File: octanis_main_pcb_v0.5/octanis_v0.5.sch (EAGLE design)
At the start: 103 parts, among them IC1 BME280, IC2 BNO055A, Q1 32.768kHz, Q2 32.768kHz, U1 MSP432, U10 INA213, U11 INA213, U12 MAX6001SOT-23, U2 TPS61232, U3 DRV8836DSSR, U4 DRV8836DSSR, U5 DRV8836DSSR, U6 DRV8836DSSR, U7 SST25VF064C, U8 INA213, U9 INA213

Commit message: renumbered parts in mainboard
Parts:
- removed LED0: LED0, adafruit:LEDCHIPLED_0603
- removed RPUC, RPUD: 4.7k, rcl:R-EU_R0603
- added LED2: LED1, adafruit:LEDCHIPLED_0603
- added R19: 10k, rcl:R-EU_R0603
- added R20: 6.8k, rcl:R-EU_R0603
- C1: value 100n -> 10u; device rcl:C-EUC0402 -> rcl:CPOL-EUA/3216-18R
- C10, C30: value 10u -> 470n; device rcl:CPOL-EUA/3216-18R -> rcl:C-EUC0603
- C12, C29: value 100n -> 470n
- C13: value 100n -> 10u; device rcl:C-EUC0603 -> rcl:CPOL-EUA/3216-18R
- C15: value 1n -> 10u; device rcl:C-EUCM0402 -> rcl:CPOL-EUA/3216-18R
- C16: value 12p -> 100n; device rcl:C-EUC0603 -> rcl:C-EUC0402
- C19, C23: value 100n -> 12p
- C2: value 100n -> 22uF
- C20: value 120n -> 100n
- C21, C24: value 10n -> 100n
- C22: value 12p -> 120n; device rcl:C-EUC0402 -> rcl:C-EUC0603
- C25: value 10u -> 12p; device rcl:CPOL-EUA/3216-18R -> rcl:C-EUC0402
- C26: value 470n -> 100n; device rcl:C-EUC0603 -> rcl:C-EUC0402
- C3, C6: value 22uF -> 100n
- C31, C32: value 10n -> 470n
- C33, C34, C35, C36: value 470n -> 10n
- C4: value 10nF -> 22uF
- C5: value 22uF -> 10nF
- C7: value 3 x 22uF -> 22uF
- C8: value 470n -> 1n; device rcl:C-EUC0603 -> rcl:C-EUCM0402
- C9: value 12p -> 3 x 22uF; device rcl:C-EUC0402 -> rcl:C-EUC0603
- LED1: value LED1 -> LED0
- R1: value 10k -> 4.7k
- R10: value 91k 0.1% ±25 ppm/°C -> 10k; device rcl:R-EU_R0402 -> rcl:R-EU_R0603
- R11: value 10k -> 0R; device rcl:R-EU_R0603 -> rcl:R-EU_R0402
- R13: value 47k -> 10k; device rcl:R-EU_RM0402 -> rcl:R-EU_R0603
- R14: value 6.8k -> 91k 0.1% ±25 ppm/°C; device rcl:R-EU_R0603 -> rcl:R-EU_R0402
- R16: value 10k -> 6.8k
- R17: value 6.8k -> 10k
- R2: value 1M -> 1k
- R3: value 1M -> 4.7k
- R4: value 1k -> 1M
- R5: value 10k -> 1M
- R7: value 0R -> 1k; device rcl:R-EU_R0402 -> rcl:R-EU_R0603
- R8: value 1k -> 47k; device rcl:R-EU_R0603 -> rcl:R-EU_RM0402
- RS1: value RS1 -> RS4
- RS2: value RS2 -> RS3
- RS3: value RS3 -> RS2
- RS4: value RS4 -> RS1
- U1: value MSP432 -> TPS61232; device MSP-EXP432:MSP432 -> texasinstruments:TPS61232
- U12: value MAX6001SOT-23 -> INA213; device Octanis1:MAX6001SOT-23 -> Octanis1_EPS:INA213
- U2: value TPS61232 -> DRV8836DSSR; device texasinstruments:TPS61232 -> DRV8834:DRV8836DSSR
- U4: value DRV8836DSSR -> MSP432; device DRV8834:DRV8836DSSR -> MSP-EXP432:MSP432
- U5: value DRV8836DSSR -> SST25VF064C; device DRV8834:DRV8836DSSR -> BertaLib:SST25VF064C
- U7: value SST25VF064C -> DRV8836DSSR; device BertaLib:SST25VF064C -> DRV8834:DRV8836DSSR
- U8: value INA213 -> MAX6001SOT-23; device Octanis1_EPS:INA213 -> Octanis1:MAX6001SOT-23
- renumbered JP4 to JP2, JP5 to JP1, LED_J1 to LED_J101, LED_J2 to LED_J100, M1/M2 to M1/M1, M3/M4 to M3/M1, M5/M6 to M5/M1, M7/M8 to M7/M1, RX2/TX2 to RX2/TX1, RX3/TX3 to RX3/TX1, U$2 to U$100, U$4 to U$1
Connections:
- net +3V3: now also C13.+, C2.1, C20.2, C21.1, C22.1, C24.1, C6.1, R1.2, R10.2, R12.1, R17.2, R19.2, R3.2, R4.2, R8.2, U1.VIN, U4.DVCC1, U4.DVCC2, U5.HOLD, U5.VCC, U5.WP, U8.IN; no longer C13.1, C14.1, C19.2, C20.1, C29.1, C3.1, C30.+, R1.1, R12.2, R16.2, R2.2, R5.2, R7.2, RPUC.2, RPUD.2, U1.DVCC1, U1.DVCC2, U12.IN, U2.VIN, U7.HOLD, U7.VCC, U7.WP
- net +5V: now also C1.+, C3.1, C4.1, C9.1, R5.2, U1.FB, U1.VOUT; no longer C10.+, C2.1, C5.1, C6.1, R3.2, U2.FB, U2.VOUT
- net 5VEN: now also R4.1, U1.EN, U4.P2.1/PM_UCA1CLK; no longer R2.1, U1.P2.1/PM_UCA1CLK, U2.EN
- net A0: now also U4.P5.5/A0; no longer U1.P5.5/A0
- net A1: now also U4.P5.4/A1; no longer U1.P5.4/A1
- net A10: now also U4.P4.3/MCLK/RTCCLK/A10; no longer U1.P4.3/MCLK/RTCCLK/A10
- net A11: now also U4.P4.2/ACLK/TA2CLK/A11; no longer U1.P4.2/ACLK/TA2CLK/A11
- net A12: now also U4.P4.1/A12; no longer U1.P4.1/A12
- net A13: now also U4.P4.0/A13; no longer U1.P4.0/A13
- net A14: now also U4.P6.1/A14; no longer U1.P6.1/A14
- net A15: now also U4.P6.0/A15; no longer U1.P6.0/A15
- net A16: now also U4.P9.1/A16; no longer U1.P9.1/A16
- net A17: now also U4.P9.0/A17; no longer U1.P9.0/A17
- net A18: now also U4.P8.7/A18; no longer U1.P8.7/A18
- net A2: now also U4.P5.3/A2; no longer U1.P5.3/A2
- net A20: now also C32.2, R20.1, U4.P8.5/A20; no longer C35.2, R17.1, U1.P8.5/A20
- net A20UNF: now also R20.2, U9.OUT; no longer R17.2, U11.OUT
- net A21: now also C28.2, U4.P8.4/A21; no longer C36.2, U1.P8.4/A21
- net A22: now also C29.2, R16.1, U4.P8.3/TA3CLK/A22; no longer C34.2, R15.1, U1.P8.3/TA3CLK/A22
- net A22UNF: now also R16.2, U11.OUT; no longer R15.2, U9.OUT
- net A23: now also C27.2, R15.1, U4.P8.2/TA3.2/A23; no longer C33.2, R14.1, U1.P8.2/TA3.2/A23
- net A23UNF: now also R15.2, U12.OUT; no longer R14.2, U8.OUT
- net A3: now also U4.P5.2/A3; no longer U1.P5.2/A3
- net A4: now also U4.P5.1/A4; no longer U1.P5.1/A4
- net A5: now also U4.P5.0/A5; no longer U1.P5.0/A5
- net A6: now also U4.P4.7/A6; no longer U1.P4.7/A6
- net A7: now also U4.P4.6/A7; no longer U1.P4.6/A7
- net A8: now also U4.P4.5/A8; no longer U1.P4.5/A8
- net A9: now also U4.P4.4/HSMCLK/SVMHOUT/A9; no longer U1.P4.4/HSMCLK/SVMHOUT/A9
- net ACCEL_INT: now also U4.P3.5/PM_UCB2CLK; no longer U1.P3.5/PM_UCB2CLK
- net ACCEL_N_BOOTLD: now also R13.1; no longer R5.1
- net ACCEL_N_RST: now also R12.2; no longer R1.2
- net AGND: now also C16.2, C26.2, C27.1, C28.1, C29.1, R14.2, U4.AVSS1, U4.AVSS2, U4.AVSS3; no longer C1.2, C21.1, C23.2, C24.1, C31.1, R10.2, U1.AVSS1, U1.AVSS2, U1.AVSS3
- net AVCC: now also C16.1, C26.1, R11.1, U4.AVCC1, U4.AVCC2; no longer C1.1, C23.1, R7.1, U1.AVCC1, U1.AVCC2
- net CURR_SENSE_EN: now also C33.2, C34.2, C35.2, C36.2, U12.VCC, U4.P8.6/A19; no longer C21.2, C24.2, C31.2, C32.2, U1.P8.6/A19, U8.VCC
- net GND: now also C10.1, C13.-, C14.1, C15.-, C19.2, C2.2, C20.1, C21.2, C22.2, C23.1, C24.2, C25.1, C30.1, C31.1, C8.2, C9.2, R6.1, R7.1, U1.GND, U1.GND1, U1.GND2, U1.GND3, U1.GND4, U1.GND5, U2.EPAD, U4.DVSS1, U4.DVSS2, U4.DVSS3, U4.P5.7/TA2.2/VREF-/VEREF-/C1.6, U7.EPAD; no longer C13.2, C14.2, C15.2, C16.2, C19.1, C20.2, C22.1, C25.-, C26.1, C27.1, C28.1, C29.2, C3.2, C30.-, C8.1, C9.1, R8.1, R9.1, U1.DVSS1, U1.DVSS2, U1.DVSS3, U1.P5.7/TA2.2/VREF-/VEREF-/C1.6, U2.GND1, U2.GND2, U2.GND3, U2.GND4, U2.GND5, U4.EPAD, U4.GND, U5.EPAD
- net HX1_DATA: now also U4.P1.4/UCB0STE; no longer U1.P1.4/UCB0STE
- net HX1_EN: now also U4.P1.5/UCB0CLK; no longer U1.P1.5/UCB0CLK
- net IND: now also U1.SW; no longer U2.SW
- net LED0: now also LED1.A, U4.P10.0/UCB3STE; no longer LED0.A, U1.P10.0/UCB3STE
- net LED1: now also LED2.A, U4.P10.1/UCB3CLK; no longer LED1.A, U1.P10.1/UCB3CLK
- net M1234SLEEP: now also R10.1, U2.MODE, U2.NSLEEP, U4.P2.2/PM_UCA1RXD/PM_UCA1SOMI; no longer R12.1, U1.P2.2/PM_UCA1RXD/PM_UCA1SOMI, U4.MODE, U4.NSLEEP
- net M1IN1: now also U2.AIN1_/_APHASE, U4.P2.3/PM_UCA1TXD/PM_UCA1SIMO; no longer U1.P2.3/PM_UCA1TXD/PM_UCA1SIMO, U3.AIN1_/_APHASE
- net M1IN2: now also U2.AIN2_/_AENBL, U4.P2.4/PM_TA0.1; no longer U1.P2.4/PM_TA0.1, U3.AIN2_/_AENBL
- net M2IN1: now also U2.BIN1_/_BPHASE, U4.P2.5/PM_TA0.2; no longer U1.P2.5/PM_TA0.2, U3.BIN1_/_BPHASE
- net M2IN2: now also U2.BIN2_/_BENBL, U4.P2.6/PM_TA0.3; no longer U1.P2.6/PM_TA0.3, U3.BIN2_/_BENBL
- net M3IN1: now also U3.AIN1_/_APHASE, U4.P2.7/PM_TA0.4; no longer U1.P2.7/PM_TA0.4, U4.AIN1_/_APHASE
- net M3IN2: now also U3.AIN2_/_AENBL, U4.P10.4/TA3.0/C0.7; no longer U1.P10.4/TA3.0/C0.7, U4.AIN2_/_AENBL
- net M4IN1: now also U3.BIN1_/_BPHASE, U4.P10.5/TA3.1/C0.6; no longer U1.P10.5/TA3.1/C0.6, U4.BIN1_/_BPHASE
- net M4IN2: now also U3.BIN2_/_BENBL, U4.P7.4/PM_TA1.4/C0.5; no longer U1.P7.4/PM_TA1.4/C0.5, U4.BIN2_/_BENBL
- net M5678SLEEP: now also R17.1, U4.P2.0/PM_UCA1STE, U7.MODE, U7.NSLEEP; no longer R11.1, U1.P2.0/PM_UCA1STE, U5.MODE, U5.NSLEEP
- net M5IN1: now also U4.P7.5/PM_TA1.3/C0.4, U7.AIN1_/_APHASE; no longer U1.P7.5/PM_TA1.3/C0.4, U5.AIN1_/_APHASE
- net M5IN2: now also U4.P7.6/PM_TA1.2/C0.3, U7.AIN2_/_AENBL; no longer U1.P7.6/PM_TA1.2/C0.3, U5.AIN2_/_AENBL
- net M5OUT1: now also RS4.I1, U7.AOUT1; no longer RS1.I1, U5.AOUT1
- net M6IN1: now also U4.P8.0/UCB3STE/TA1.0/C0.1, U7.BIN1_/_BPHASE; no longer U1.P8.0/UCB3STE/TA1.0/C0.1, U5.BIN1_/_BPHASE
- net M6IN2: now also U4.P7.7/PM_TA1.1/C0.2, U7.BIN2_/_BENBL; no longer U1.P7.7/PM_TA1.1/C0.2, U5.BIN2_/_BENBL
- net M7IN1: now also U4.P8.1/UCB3CLK/TA2.0/C0.0; no longer U1.P8.1/UCB3CLK/TA2.0/C0.0
- net M7IN2: now also U4.P3.0/PM_UCA2STE; no longer U1.P3.0/PM_UCA2STE
- net M8IN1: now also U4.P3.1/PM_UCA2CLK; no longer U1.P3.1/PM_UCA2CLK
- net M8IN2: now also U4.P3.4/PM_UCB2STE; no longer U1.P3.4/PM_UCB2STE
- net N$1: now also C14.2, C15.+, U4.VCORE; no longer C18.2, C25.+, U1.VCORE
- net N$10: now also C25.2, U4.PJ.1/LFXOUT; no longer C9.2, U1.PJ.1/LFXOUT
- net N$13: now also U3.AOUT1; no longer U4.AOUT1
- net N$14: now also R2.1; no longer R6.1
- net N$15: now also RS4.V2, U12.IN-; no longer RS1.V2, U8.IN-
- net N$17: now also RS4.V1, U12.IN+; no longer RS1.V1, U8.IN+
- net N$18: now also C18.2; no longer C12.2
- net N$19: now also C19.1; no longer C16.1
- net N$2: now also R5.1, U1.PG; no longer R3.1, U2.PG
- net N$21: now also RS4.I2; no longer RS1.I2
- net N$23: now also RS3.V1, U11.IN+; no longer RS2.V1, U9.IN+
- net N$24: now also RS3.V2, U11.IN-; no longer RS2.V2, U9.IN-
- net N$25: now also RS3.I1, U7.BOUT1; no longer RS2.I1, U5.BOUT1
- net N$26: now also R9.1; no longer R4.1
- net N$27: now also RS3.I2; no longer RS2.I2
- net N$28: now also RS2.V2; no longer RS3.V2
- net N$29: now also RS2.V1; no longer RS3.V1
- net N$30: now also RS1.V2, U9.IN-; no longer RS4.V2, U11.IN-
- net N$31: now also RS1.V1, U9.IN+; no longer RS4.V1, U11.IN+
- net N$32: now also RS2.I2; no longer RS3.I2
- net N$33: now also R14.1, U4.DCOR; no longer R10.1, U1.DCOR
- net N$34: now also U4.VSW; no longer U1.VSW
- net N$35: now also RS1.I1; no longer RS4.I1
- net N$36: now also RS2.I1; no longer RS3.I1
- net N$37: now also RS1.I2; no longer RS4.I2
- net N$38: now also U7.AOUT2; no longer U5.AOUT2
- net N$39: now also U3.AOUT2; no longer U4.AOUT2
- net N$4: now also R9.2; no longer R4.2
- net N$40: now also U3.BOUT1; no longer U4.BOUT1
- net N$41: now also U3.BOUT2; no longer U4.BOUT2
- net N$42: now also C5.1, U1.SS; no longer C4.1, U2.SS
- net N$43: now also U7.BOUT2; no longer U5.BOUT2
- net N$44: now also R2.2; no longer R6.2
- net N$49: now also U2.AOUT1; no longer U3.AOUT1
- net N$5: now also LED1.C, R7.2; no longer LED0.C, R8.2
- net N$50: now also U2.AOUT2; no longer U3.AOUT2
- net N$51: now also U2.BOUT1; no longer U3.BOUT1
- net N$52: now also U2.BOUT2; no longer U3.BOUT2
- net N$6: now also LED2.C, R6.2; no longer LED1.C, R9.2
- net N$76: now also U4.SWDIOTMS; no longer U1.SWDIOTMS
- net N$77: now also U4.SWCLKTCK; no longer U1.SWCLKTCK
- net N$8: now also C23.2, U4.PJ.0/LFXIN; no longer C22.2, U1.PJ.0/LFXIN
- net P1.0: now also U4.P1.0/UCA0STE; no longer U1.P1.0/UCA0STE
- net P1.1: now also U4.P1.1/UCA0CLK; no longer U1.P1.1/UCA0CLK
- net P10.2: now also U4.P10.2/UCB3SIMO/UCB3SDA; no longer U1.P10.2/UCB3SIMO/UCB3SDA
- net P10.3: now also U4.P10.3UCB3SOMI/UCB3SCL; no longer U1.P10.3UCB3SOMI/UCB3SCL
- net P3.6: now also U4.P3.6/PM_UCB2SIMO/PM_UCB2SDA; no longer U1.P3.6/PM_UCB2SIMO/PM_UCB2SDA
- net P3.7: now also U4.P3.7/PM_UCB2SOMI/PM_UCB2SCL; no longer U1.P3.7/PM_UCB2SOMI/PM_UCB2SCL
- net P6.6: now also U4.P6.6/TA2.3/UCB3SIMO/UCB3SDA/C1.1; no longer U1.P6.6/TA2.3/UCB3SIMO/UCB3SDA/C1.1
- net P6.7: now also U4.P6.7/TA2.4/UCB3SOMI/UCB3SCL/C1.0; no longer U1.P6.7/TA2.4/UCB3SOMI/UCB3SCL/C1.0
- net P7.0: now also U4.P7.0/PM_SMCLK/PM_DMAE0; no longer U1.P7.0/PM_SMCLK/PM_DMAE0
- net P7.1: now also U4.P7.1/PM_C0OUT/PM_TA0CLK; no longer U1.P7.1/PM_C0OUT/PM_TA0CLK
- net P7.2: now also U4.P7.2/PM_C1OUT/PM_TA1CLK; no longer U1.P7.2/PM_C1OUT/PM_TA1CLK
- net P7.3: now also U4.P7.3/PM_TA0.0; no longer U1.P7.3/PM_TA0.0
- net P9.2: now also U4.P9.2/TA3.3; no longer U1.P9.2/TA3.3
- net P9.3: now also U4.P9.3/TA3.4; no longer U1.P9.3/TA3.4
- net P9.4: now also U4.P9.4/UCA3STE; no longer U1.P9.4/UCA3STE
- net P9.5: now also U4.P9.5/UCA3CLK; no longer U1.P9.5/UCA3CLK
- net PJ.2: now also U4.PJ.2/HFXOUT; no longer U1.PJ.2/HFXOUT
- net PJ.3: now also U4.PJ.3/HFXIN; no longer U1.PJ.3/HFXIN
- net PJ.4: now also U4.PJ.4/TDI/ADC14CLK; no longer U1.PJ.4/TDI/ADC14CLK
- net PJ.5: now also U4.PJ.5/TDO/SWO; no longer U1.PJ.5/TDO/SWO
- net RFGND: now also C1.-, C3.2; no longer C10.-, C2.2
- net RST_N: now also C8.1, R8.1, U4.RSTN/NMI; no longer C15.1, R13.1, U1.RSTN/NMI
- net RX0: now also U4.P1.2/UCA0RXD/UCA0SOMI; no longer U1.P1.2/UCA0RXD/UCA0SOMI
- net RX2: now also U4.P3.2/PM_UCA2RXD/PM_UCA2SOMI; no longer U1.P3.2/PM_UCA2RXD/PM_UCA2SOMI
- net RX3: now also U4.P9.6/UCA3RXD/UCA3SOMI; no longer U1.P9.6/UCA3RXD/UCA3SOMI
- net SCL: now also R1.1, U4.P1.7/UCB0SOMI/UCB0SCL; no longer RPUD.1, U1.P1.7/UCB0SOMI/UCB0SCL
- net SDA: now also R3.1, U4.P1.6/UCB0SIMO/UCB0SDA; no longer RPUC.1, U1.P1.6/UCB0SIMO/UCB0SDA
- net SPI_EXTSLAVE_TE: now also U4.P6.2/UCB1STE/C1.5; no longer U1.P6.2/UCB1STE/C1.5
- net SPI_FLASH_CS: now also R19.1, U4.P5.6/TA2.1/VREF+/VEREF+/C1.7, U5.CS; no longer R16.1, U1.P5.6/TA2.1/VREF+/VEREF+/C1.7, U7.CS
- net SPI_MISO: now also U4.P6.5/UCB1SOMI/UCB1SCL/C1.2, U5.MISO; no longer U1.P6.5/UCB1SOMI/UCB1SCL/C1.2, U7.MISO
- net SPI_MOSI: now also U4.P6.4/UCB1SIMO/UCB1SDA/C1.3, U5.MOSI; no longer U1.P6.4/UCB1SIMO/UCB1SDA/C1.3, U7.MOSI
- net SPI_SCK: now also U4.P6.3/UCB1CLK/C1.4, U5.SCK; no longer U1.P6.3/UCB1CLK/C1.4, U7.SCK
- net TX0: now also U4.P1.3/UCA0TXD/UCA0SIMO; no longer U1.P1.3/UCA0TXD/UCA0SIMO
- net TX2: now also U4.P3.3/PM_UCA2TXD/PM_UCA2SIMO; no longer U1.P3.3/PM_UCA2TXD/PM_UCA2SIMO
- net TX3: now also U4.P9.7/UCA3TXD/UCA3SIMO; no longer U1.P9.7/UCA3TXD/UCA3SIMO
- net VREF_M: now also U12.REF, U8.OUT; no longer U12.OUT, U8.REF
- net V_MOTOR: now also C10.2, C12.2, U2.VCC; no longer C27.2, C28.2, U4.VCC
- net V_MOTOR2: now also C30.2, C31.2, U7.VCC; no longer C26.2, C8.2, U5.VCC
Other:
- moved on the sheet: C11, C12, C14, C16, C18, C19, C2, C20, C21, C22, C23, C24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

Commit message: added RN2483 LoRa module, separated 3v supply for motors and 5V converter from main circuit supply. *
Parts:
- removed C1: 10u, rcl:CPOL-EUA/3216-18R
- removed C3: 100n, rcl:C-EUC0603
- removed MOT_J, RF_J: (no value), jumper:SJ
- removed PROG: (no value), Headerlibrary:PINHD-1X72MM
- removed R10, R17: 10k, rcl:R-EU_R0603
- removed RX3/TX1: (no value), pinhead:PINHD-2X2
- removed U$1: HX1EXTERNALMOUNT, Octanis1:HX1EXTERNALMOUNT
- added 433MHZ, 868MHZ, LORA_RST_N: (no value), Headerlibrary:PINHD-1X1
- added J1: (no value), Seeed-OPL-Connector:SMD-BLUE-FEMALE-HEADER-VERT(2X3P-2.54)
- added MOT_J1: (no value), jumper:SJ
- added R21: 100k, rcl:R-EU_R0603
- added RX1/TX1: (no value), pinhead-2:PINHD-1X04_2.54-S
- added U13: RN2483, Octanis1:RN2483
- added VMOT_SEL2: 3V3 V_Motor 5V, jumper:SJ2W
- JP1: device pinhead:PINHD-2X2 -> Headerlibrary:PINHD-1X72MM_SMD
- R12, R13: value 10k -> 100k
- renumbered M1/M1 to M1/M2, M3/M1 to M3/M4, RX2/TX1 to RX2/TX2
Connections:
- removed net HX1_DATA: U$1.TXD, U4.P1.4/UCB0STE
- removed net HX1_EN: U$1.EN, U4.P1.5/UCB0CLK
- removed net P1.1: DIGITAL_IO.21, U4.P1.1/UCA0CLK
- removed net P10.3: DIGITAL_IO.22, U4.P10.3UCB3SOMI/UCB3SCL
- removed net P3.6: DIGITAL_IO.5, U4.P3.6/PM_UCB2SIMO/PM_UCB2SDA
- removed net RFGND: C1.-, C3.2, RF_J.2, U$1.0V, U$1.RFGND, U$1.RFGND2
- new net 3V3_MODULE2: C2.1, JP2.10, JP2.9, L1.1, R4.2, U1.VIN, U8.IN, VMOT_SEL.1, VMOT_SEL2.1
- new net ANT433: 433MHZ.1, U13.P$25
- new net ANT868: 868MHZ.1, U13.P$23
- new net EXT_LIGHTNING_INT: J1.6, U4.P1.4/UCB0STE
- new net EXT_UV_EN: J1.1, U4.P1.5/UCB0CLK
- new net LORA_RST_N: LORA_RST_N.1, R21.1, U13.P$32
- new net N$20: MOT_J1.1, R4.1, U1.EN
- new net P5.7: DIGITAL_IO.5, U4.P5.7/TA2.2/VREF-/VEREF-/C1.6
- new net RX1: RX1/TX1.3, U4.P2.2/PM_UCA1RXD/PM_UCA1SOMI
- new net TX1: RX1/TX1.2, U4.P2.3/PM_UCA1TXD/PM_UCA1SIMO
- net +3V3: now also DIGITAL_IO.21, J1.2, JP1.7, JP2.3, JP2.4, R21.2, RX1/TX1.4, U13.P$12, U13.P$34; no longer C2.1, JP1.1, JP2.10, JP2.7, JP2.8, JP2.9, L1.1, PROG.7, R10.2, R17.2, R4.2, RX2/TX2.1, RX3/TX1.3, U1.VIN, U8.IN, VMOT_SEL.1
- net +5V: now also RX2/TX2.4, VMOT_SEL2.3; no longer C1.+, C3.1, MOT_J.2, U$1.VCC
- net 5VEN: now also MOT_J1.2; no longer R4.1, U1.EN
- net ACCEL_INT: now also U4.P1.1/UCA0CLK; no longer U4.P3.5/PM_UCB2CLK
- net ACCEL_N_RST: now also U4.P10.3UCB3SOMI/UCB3SCL
- net GND: now also DIGITAL_IO.22, J1.5, JP1.1, JP2.7, JP2.8, RX1/TX1.1, RX2/TX2.1, U13.P$1, U13.P$11, U13.P$20, U13.P$21, U13.P$22, U13.P$24, U13.P$26, U13.P$27, U13.P$28, U13.P$33, U13.P$41, U13.P$47, U13.P$8; no longer JP1.2, JP2.3, JP2.4, PROG.1, RF_J.1, RX2/TX2.4, RX3/TX1.1, U4.P5.7/TA2.2/VREF-/VEREF-/C1.6
- net M1234SLEEP: now also U4.P2.0/PM_UCA1STE; no longer R10.1, U4.P2.2/PM_UCA1RXD/PM_UCA1SOMI
- net M1IN1: now also U4.P3.6/PM_UCB2SIMO/PM_UCB2SDA; no longer U4.P2.3/PM_UCA1TXD/PM_UCA1SIMO
- net M5678SLEEP: now also U4.P3.5/PM_UCB2CLK; no longer R17.1, U4.P2.0/PM_UCA1STE
- net N$76: now also JP1.6; no longer PROG.6
- net N$77: now also JP1.5; no longer PROG.5
- net RST_N: now also JP1.4; no longer PROG.4
- net RX0: now also JP1.2; no longer PROG.2
- net RX3: now also U13.P$6; no longer RX3/TX1.2
- net SCL: now also J1.3; no longer JP1.3
- net SDA: now also J1.4; no longer JP1.4
- net TX0: now also JP1.3; no longer PROG.3
- net TX3: now also U13.P$7; no longer RX3/TX1.4
- net V_MOTOR2: now also VMOT_SEL2.2; no longer MOT_J.1
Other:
- note removed: "Change history v0.5: --> SCHEMATIC: - added 10uF cap - connected 0V pin to RF GND - connected filter caps to RF GND --> LAYOUT: - Starground connection point placed directly at the supply pin. - Groundplane polygon around all pins with greater isolation space."
- moved on the sheet: R4

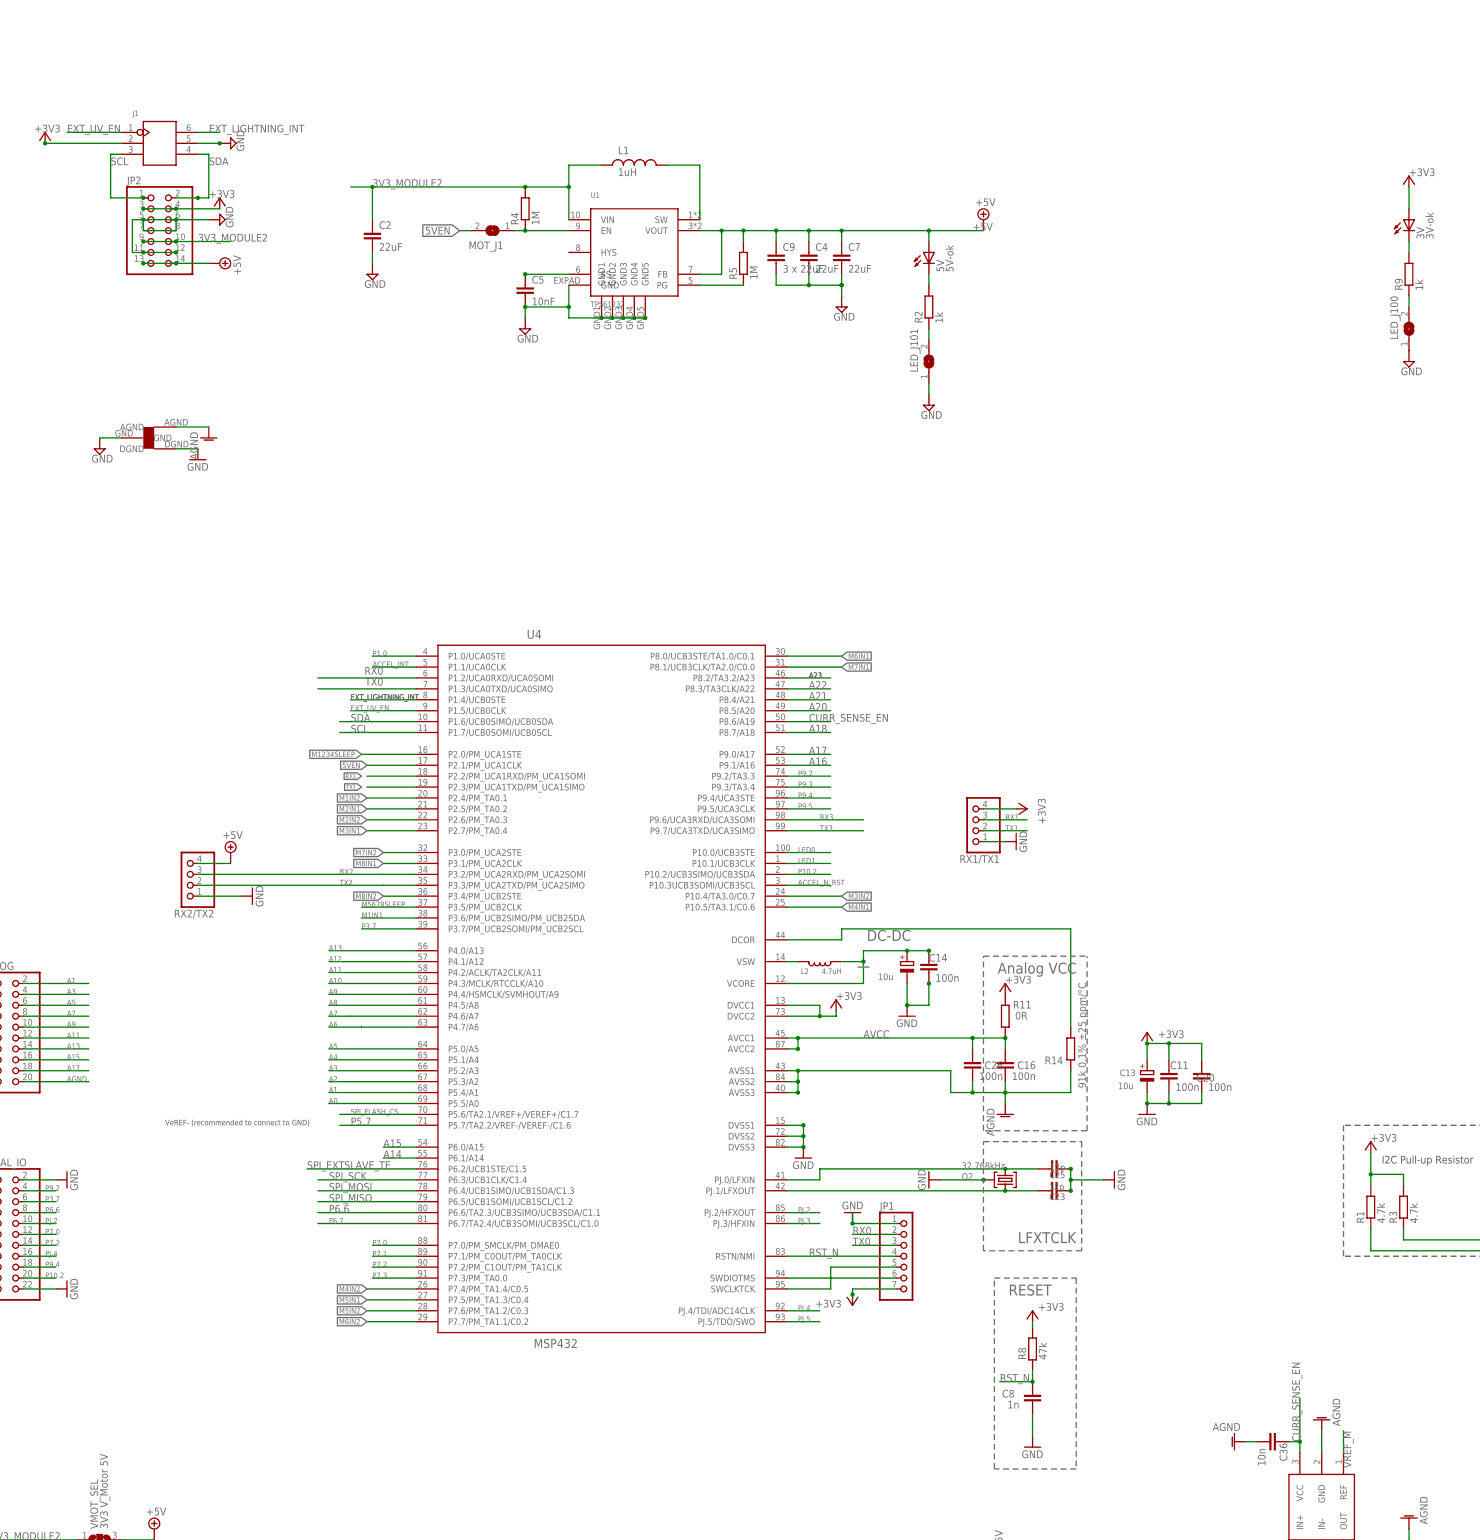
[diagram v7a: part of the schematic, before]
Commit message: finished mainboard v0.5 silkscreen
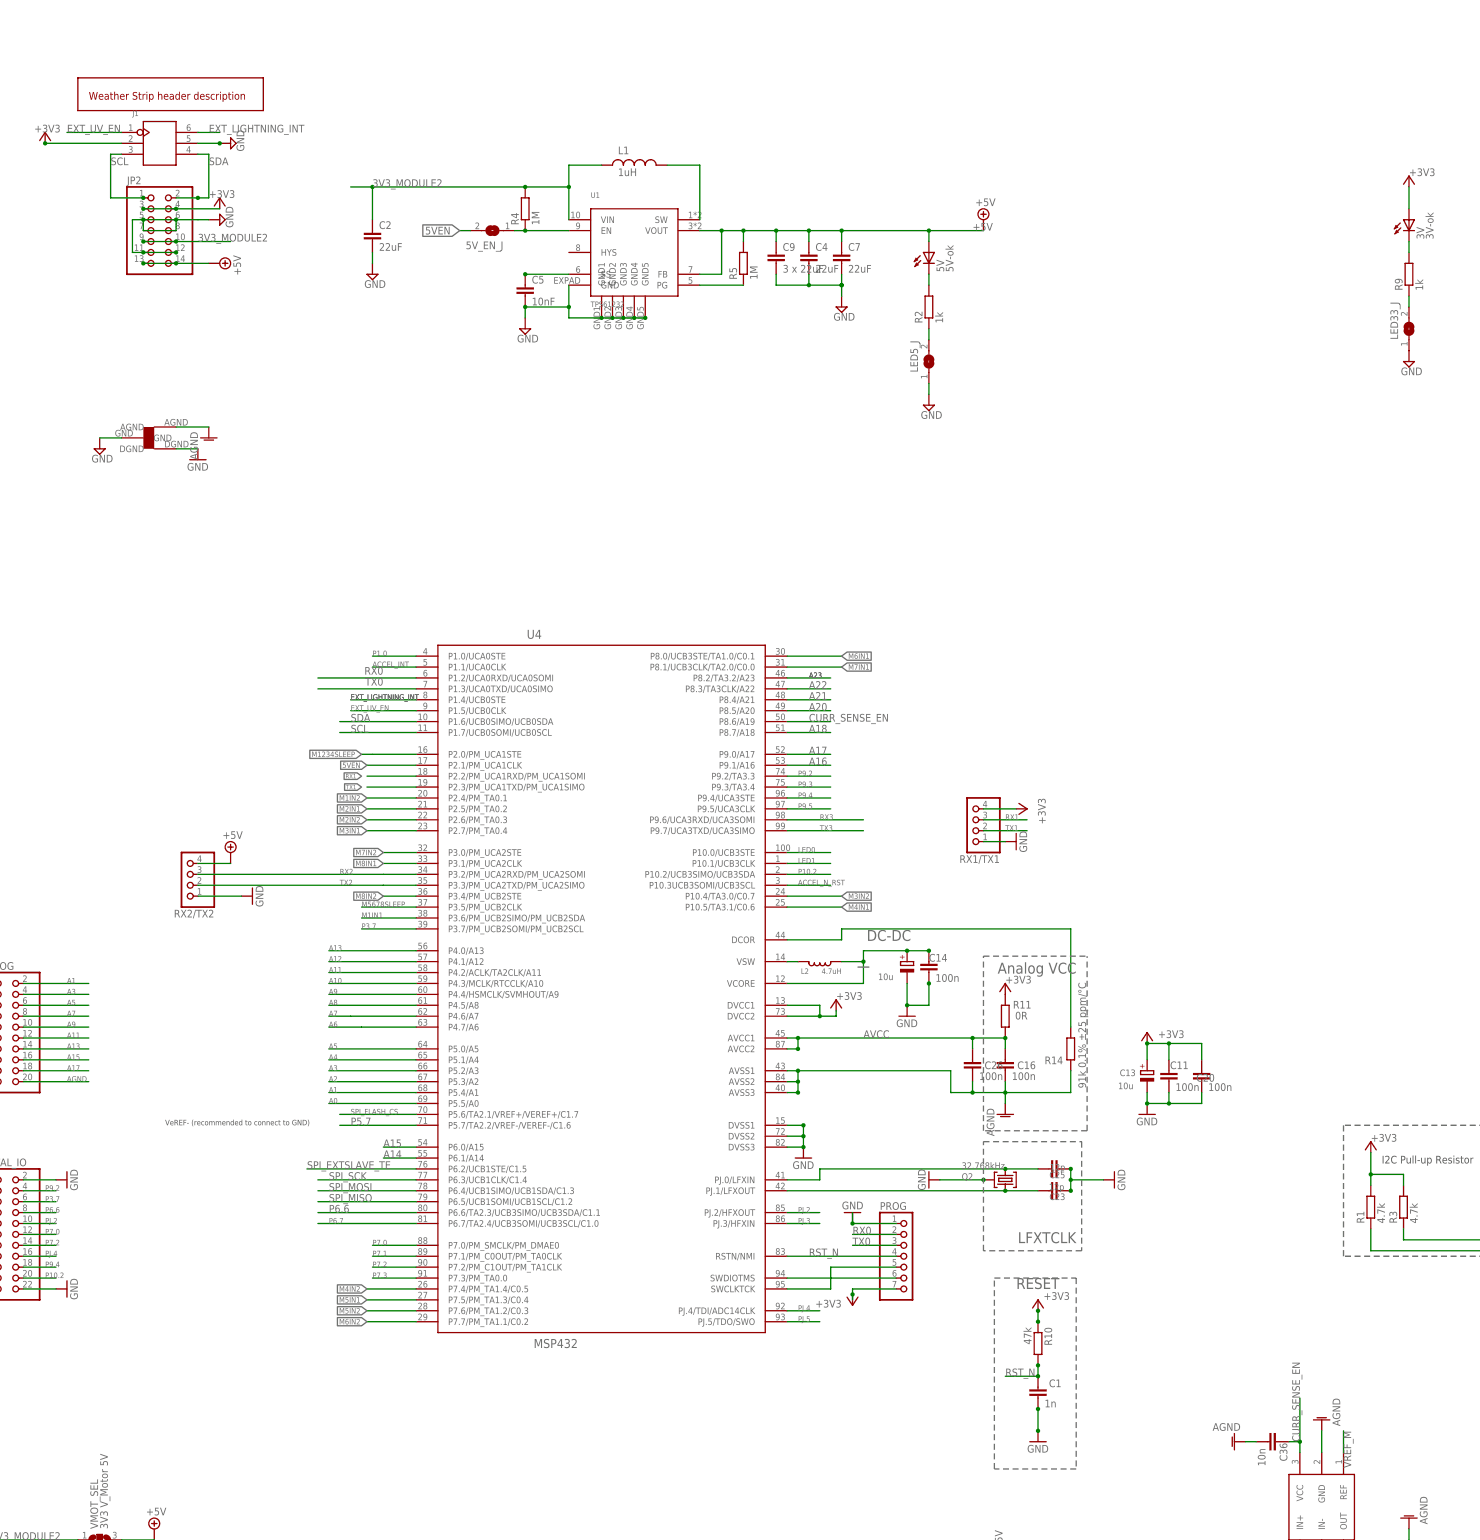
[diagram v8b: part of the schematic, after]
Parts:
- removed C8: 1n, rcl:C-EUCM0402
- removed R8: 47k, rcl:R-EU_RM0402
- added C1: 1n, rcl:C-EUC0603
- added R10: 47k, rcl:R-EU_R0603
- added U$1: WEATHER_STRIP_DOCU, Octanis1:WEATHER_STRIP_DOCU
- U10, U11, U12, U9: value INA213 -> INA210
- renumbered JP1 to PROG, LED_J100 to LED33_J, LED_J101 to LED5_J, MOT_J1 to 5V_EN_J
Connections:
- net +3V3: now also R10.1; no longer R8.2
- net GND: now also C1.1; no longer C8.2
- net RST_N: now also C1.2, R10.2; no longer C8.1, R8.1
